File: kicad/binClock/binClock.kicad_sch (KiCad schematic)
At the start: 2 parts, among them U1 ESP32-C3_SUPERMINI, U2 LOGIC-74HC595N_DIP16_

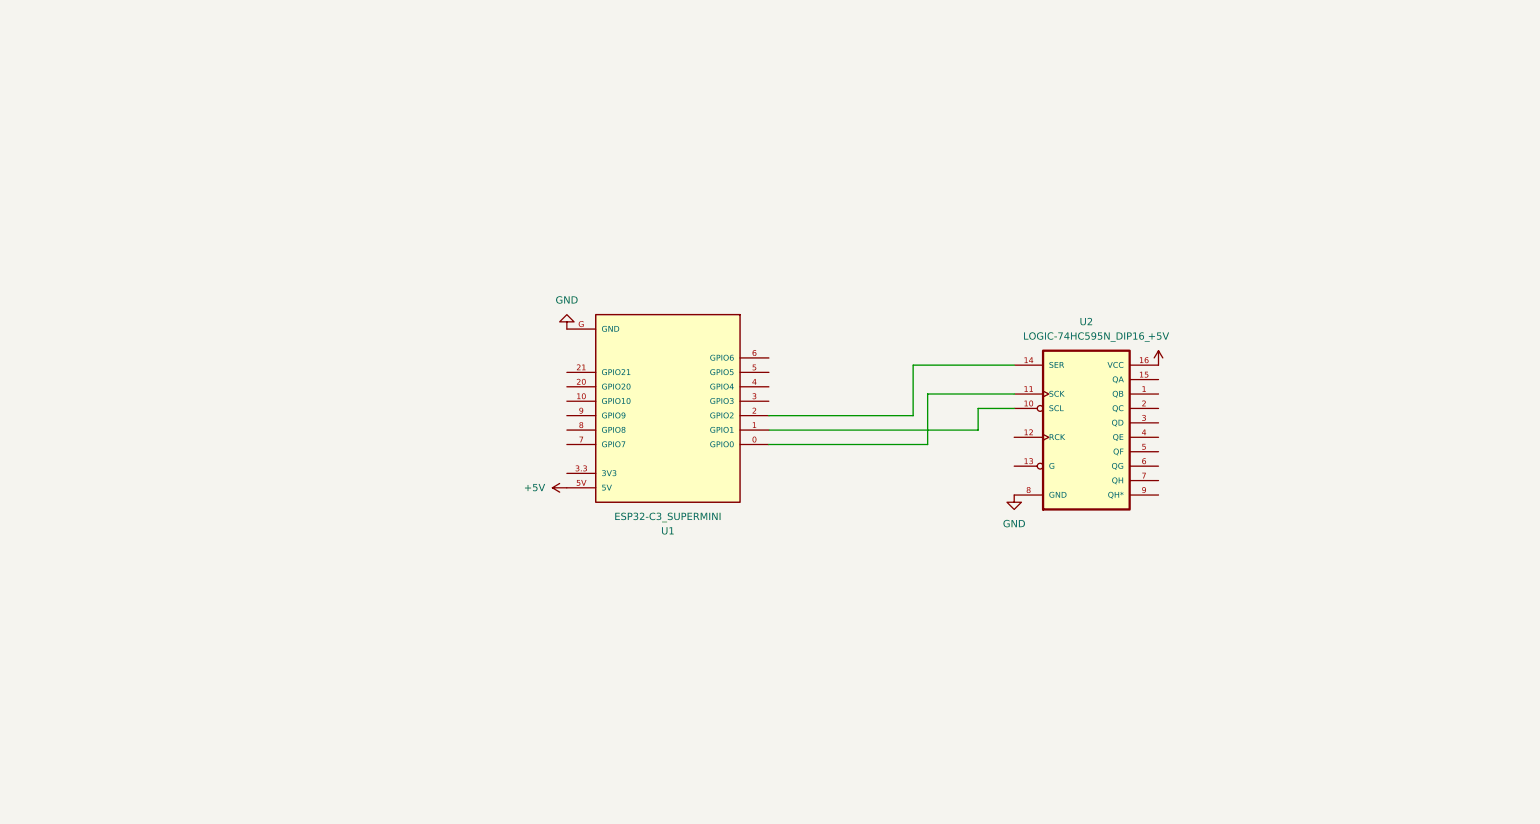
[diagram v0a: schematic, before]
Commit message: Work on schematic, added chip image
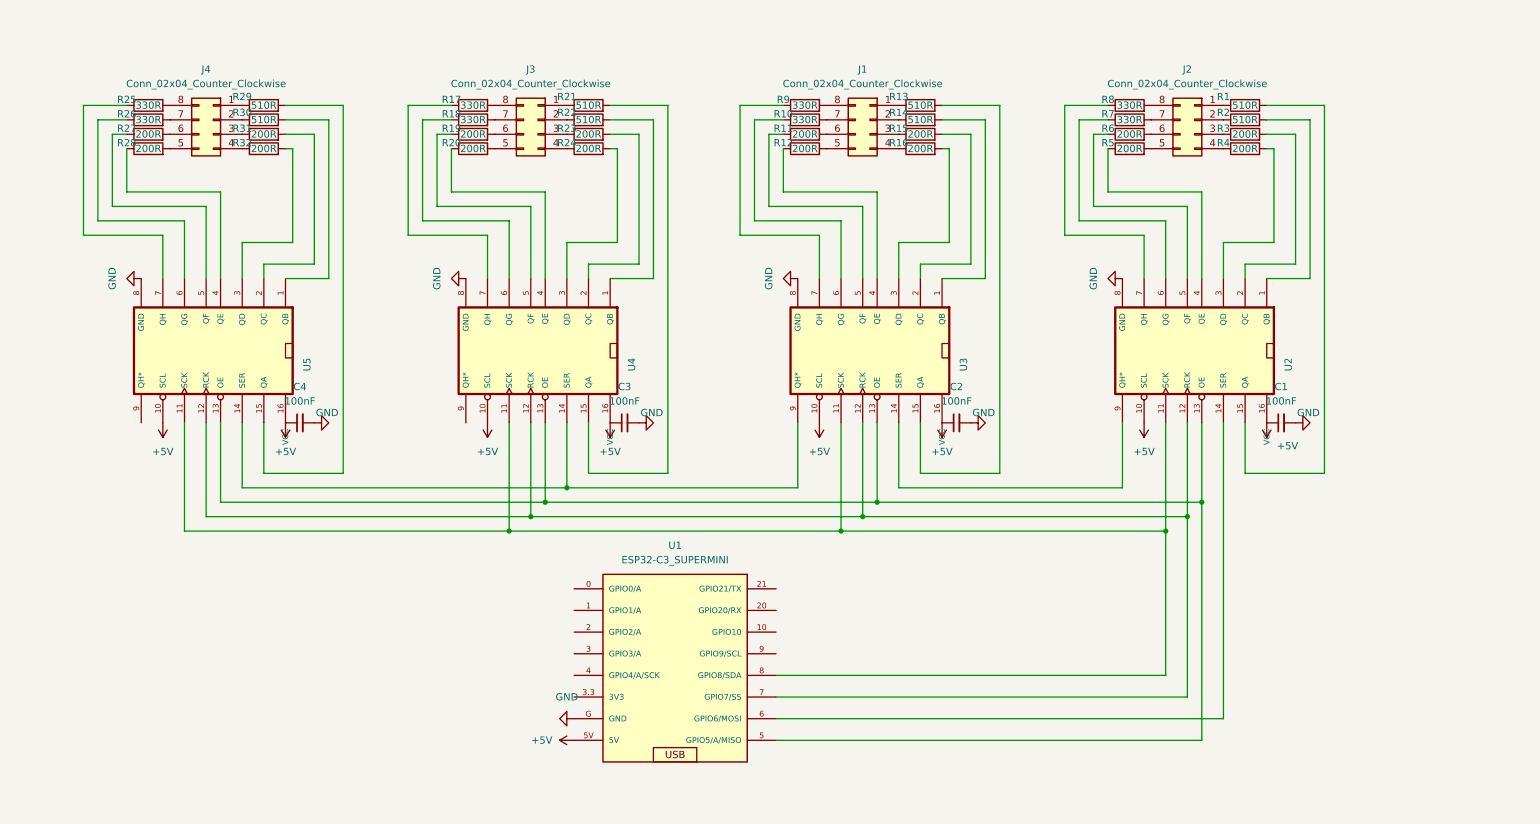
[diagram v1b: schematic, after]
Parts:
- removed U2: LOGIC-74HC595N_DIP16_, footprints:DIP16-2.54-20.32X5.84MM, symbol LOGIC-74HC595N_DIP16_:LOGIC-74HC595N_DIP16_
- added C1, C2, C3, C4: 100nF, Capacitor_THT:C_Disc_D4.3mm_W1.9mm_P5.00mm, symbol Device:C_Small
- added J1, J2, J3, J4: Conn_02x04_Counter_Clockwise, Connector_PinHeader_2.54mm:PinHeader_2x04_P2.54mm_Vertical, symbol Connector_Generic:Conn_02x04_Counter_Clockwise
- added R1, R13, R14, R2, R21, R22, R29, R30: 510R, Resistor_THT:R_Axial_DIN0207_L6.3mm_D2.5mm_P10.16mm_Horizontal, symbol Device:R
- added R10, R17, R18, R25, R26, R7, R8, R9: 330R, Resistor_THT:R_Axial_DIN0207_L6.3mm_D2.5mm_P10.16mm_Horizontal, symbol Device:R
- added R11, R12, R15, R16, R19, R20, R23, R24, R27, R28, R3, R31, R32, R4, R5, R6: 200R, Resistor_THT:R_Axial_DIN0207_L6.3mm_D2.5mm_P10.16mm_Horizontal, symbol Device:R
- added U2, U3, U4, U5: ~, symbol LOGIC-74HC595N_DIP16_:74HC595N_DIP16
- U1: footprint footprints:MODULE_ESP32-C3_SUPERMINI -> (none); Availability Not in stock -> (none); Check_prices https://www.snapeda.com/parts/ESP32-C3%20SuperMini/Espressi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 -> (none); Description_1 Super tiny ESP32-C3 board -> (none); MANUFACTURER Espressif -> (none); MAXIMUM_PACKAGE_HEIGHT 4.2mm -> (none); MF Espressif Systems -> (none); MP ESP32-C3 SuperMini -> (none); Package Package -> (none); Price None -> (none); STANDARD Manufacturer Recommendations -> (none); SnapEDA_Link https://www.snapeda.com/parts/ESP32-C3%20SuperMini/Espressi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 -> (none)
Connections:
- net +5V: now also C1.1, C2.1, C3.1, C4.1, U2.10 (SCL), U3.10 (SCL), U4.10 (SCL), U5.10 (SCL)
- net GND: now also C1.2, C2.2, C3.2, C4.2, U2.8 (GND), U3.8 (GND), U4.8 (GND), U5.8 (GND)
- net at U1.5 (GPIO5/A/MISO): now also U2.13 (OE), U3.13 (OE), U4.13 (OE), U5.13 (OE)
- net at U1.6 (GPIO6/MOSI): now also U2.14 (SER)
- net at U1.7 (GPIO7/SS): now also U2.12 (RCK), U3.12 (RCK), U4.12 (RCK), U5.12 (RCK)
- net at U1.8 (GPIO8/SDA): now also U2.11 (SCK), U3.11 (SCK), U4.11 (SCK), U5.11 (SCK)
- new net: R6.1, U2.5 (QF)
- new net: J2.6 (Pin_6), R6.2
- new net: J3.2 (Pin_2), R22.1
- new net: R22.2, U4.1 (QB)
- new net: R10.1, U3.6 (QG)
- new net: J1.7 (Pin_7), R10.2
- new net: J3.1 (Pin_1), R21.1
- new net: J3.3 (Pin_3), R23.1
- new net: J3.4 (Pin_4), R24.1
- new net: J3.5 (Pin_5), R20.2
- new net: J3.6 (Pin_6), R19.2
- new net: J3.7 (Pin_7), R18.2
- new net: J3.8 (Pin_8), R17.2
- new net: R19.1, U4.5 (QF)
- new net: R25.1, U5.7 (QH)
- new net: J4.8 (Pin_8), R25.2
- new net: J2.4 (Pin_4), R4.1
- new net: R4.2, U2.3 (QD)
- new net: J1.4 (Pin_4), R16.1
- new net: R16.2, U3.3 (QD)
- new net: R14.2, U3.1 (QB)
- new net: U2.9 (QH*), U3.14 (SER)
- new net: R13.2, U3.15 (QA)
- new net: R15.2, U3.2 (QC)
- new net: R12.1, U3.4 (QE)
- new net: R11.1, U3.5 (QF)
- new net: R9.1, U3.7 (QH)
- new net: U3.9 (QH*), U4.14 (SER), U5.14 (SER)
- new net: J1.6 (Pin_6), R11.2
- new net: R28.1, U5.4 (QE)
- new net: J4.5 (Pin_5), R28.2
- new net: R8.1, U2.7 (QH)
- new net: J2.8 (Pin_8), R8.2
- new net: R5.1, U2.4 (QE)
- new net: J2.5 (Pin_5), R5.2
- new net: J1.2 (Pin_2), R14.1
- new net: J1.3 (Pin_3), R15.1
- new net: R27.1, U5.5 (QF)
- new net: J4.6 (Pin_6), R27.2
- new net: J4.4 (Pin_4), R32.1
- new net: R32.2, U5.3 (QD)
- new net: J1.1 (Pin_1), R13.1
- new net: J1.5 (Pin_5), R12.2
- new net: J1.8 (Pin_8), R9.2
- new net: R20.1, U4.4 (QE)
- new net: R17.1, U4.7 (QH)
- new net: R23.2, U4.2 (QC)
- new net: J4.1 (Pin_1), R29.1
- new net: R29.2, U5.15 (QA)
- new net: R26.1, U5.6 (QG)
- new net: J4.7 (Pin_7), R26.2
- new net: R21.2, U4.15 (QA)
- new net: J2.1 (Pin_1), R1.1
- new net: J2.2 (Pin_2), R2.1
- new net: J2.3 (Pin_3), R3.1
- new net: J2.7 (Pin_7), R7.2
- new net: R24.2, U4.3 (QD)
- new net: J4.3 (Pin_3), R31.1
- new net: R31.2, U5.2 (QC)
- new net: R7.1, U2.6 (QG)
- new net: J4.2 (Pin_2), R30.1
- new net: R30.2, U5.1 (QB)
- new net: R2.2, U2.1 (QB)
- new net: R18.1, U4.6 (QG)
- new net: R3.2, U2.2 (QC)
- new net: R1.2, U2.15 (QA)

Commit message: Finished schematic and board layout. Included gerbers. Ordered board from jlcpcb.
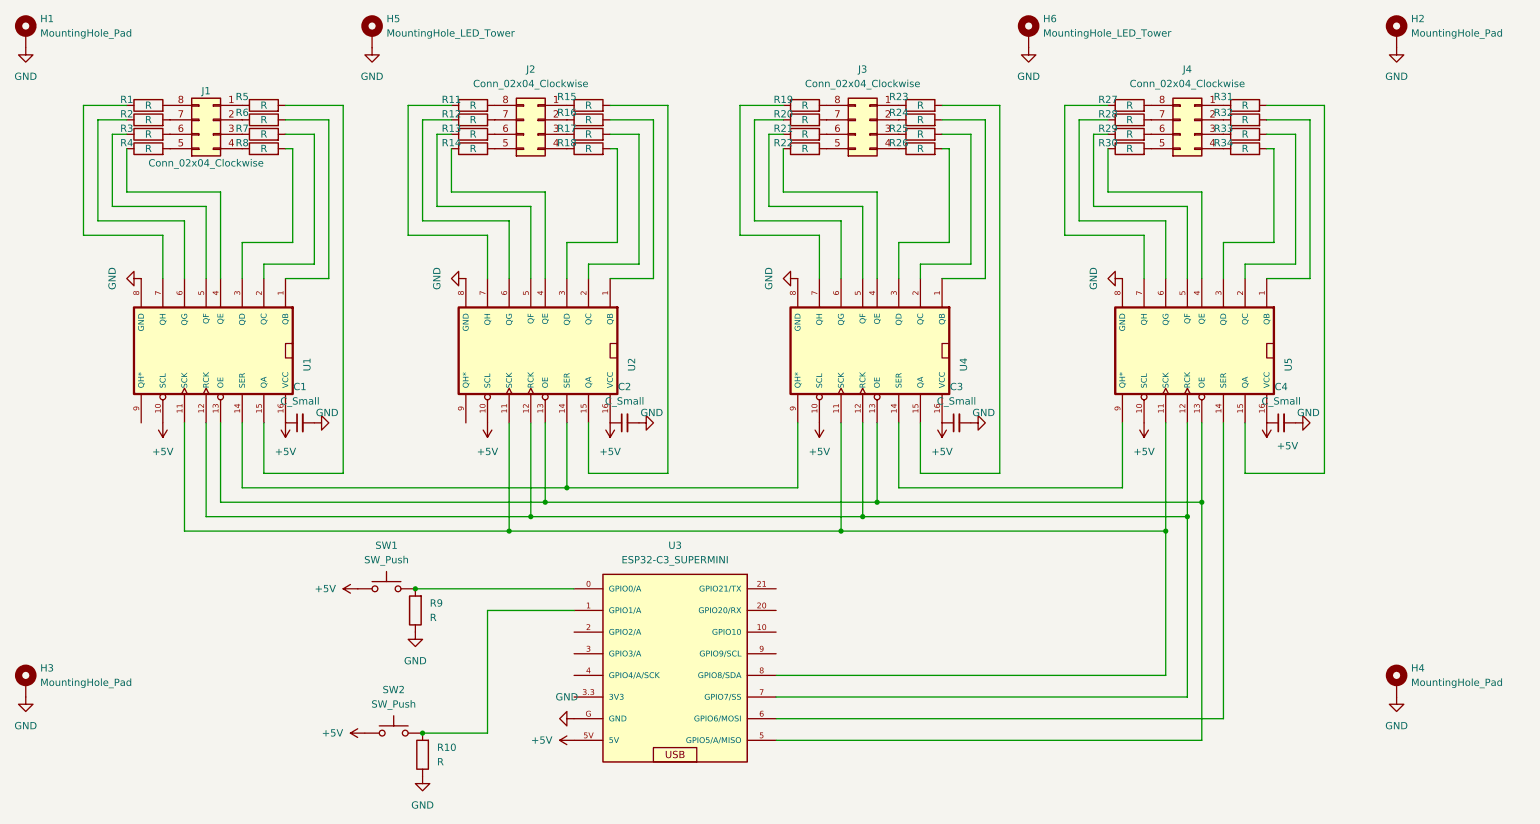
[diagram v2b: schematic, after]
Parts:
- added H1, H2, H3, H4: MountingHole_Pad, MountingHole:MountingHole_2.7mm_M2.5_Pad_TopBottom, symbol Mechanical:MountingHole_Pad
- added H5, H6: MountingHole_LED_Tower, MountingHole:MountingHole_2.2mm_M2_Pad_TopBottom, symbol Mechanical:MountingHole_Pad
- added R10, R9: R, Resistor_THT:R_Axial_DIN0207_L6.3mm_D2.5mm_P7.62mm_Horizontal, symbol Device:R
- added SW1, SW2: SW_Push, Button_Switch_THT:SW_PUSH_6mm, symbol Switch:SW_Push
- C1: renamed from C4; value 100nF -> C_Small; footprint Capacitor_THT:C_Disc_D4.3mm_W1.9mm_P5.00mm -> Capacitor_THT:C_Disc_D3.0mm_W1.6mm_P2.50mm
- C2: renamed from C3; value 100nF -> C_Small; footprint Capacitor_THT:C_Disc_D4.3mm_W1.9mm_P5.00mm -> Capacitor_THT:C_Disc_D3.0mm_W1.6mm_P2.50mm
- C3: renamed from C2; value 100nF -> C_Small; footprint Capacitor_THT:C_Disc_D4.3mm_W1.9mm_P5.00mm -> Capacitor_THT:C_Disc_D3.0mm_W1.6mm_P2.50mm
- C4: renamed from C1; value 100nF -> C_Small; footprint Capacitor_THT:C_Disc_D4.3mm_W1.9mm_P5.00mm -> Capacitor_THT:C_Disc_D3.0mm_W1.6mm_P2.50mm
- J1: renamed from J4; value Conn_02x04_Counter_Clockwise -> Conn_02x04_Clockwise; footprint Connector_PinHeader_2.54mm:PinHeader_2x04_P2.54mm_Vertical -> footprints:PinHeader_2x04_P2.54mm_Vertical_Clockwise; symbol Connector_Generic:Conn_02x04_Counter_Clockwise -> conn_02x04_clockwise:Conn_02x04_Clockwise
- J2: renamed from J3; value Conn_02x04_Counter_Clockwise -> Conn_02x04_Clockwise; footprint Connector_PinHeader_2.54mm:PinHeader_2x04_P2.54mm_Vertical -> footprints:PinHeader_2x04_P2.54mm_Vertical_Clockwise; symbol Connector_Generic:Conn_02x04_Counter_Clockwise -> conn_02x04_clockwise:Conn_02x04_Clockwise
- J3: renamed from J1; value Conn_02x04_Counter_Clockwise -> Conn_02x04_Clockwise; footprint Connector_PinHeader_2.54mm:PinHeader_2x04_P2.54mm_Vertical -> footprints:PinHeader_2x04_P2.54mm_Vertical_Clockwise; symbol Connector_Generic:Conn_02x04_Counter_Clockwise -> conn_02x04_clockwise:Conn_02x04_Clockwise
- J4: renamed from J2; value Conn_02x04_Counter_Clockwise -> Conn_02x04_Clockwise; footprint Connector_PinHeader_2.54mm:PinHeader_2x04_P2.54mm_Vertical -> footprints:PinHeader_2x04_P2.54mm_Vertical_Clockwise; symbol Connector_Generic:Conn_02x04_Counter_Clockwise -> conn_02x04_clockwise:Conn_02x04_Clockwise
- R1: renamed from R25; value 330R -> R; footprint Resistor_THT:R_Axial_DIN0207_L6.3mm_D2.5mm_P10.16mm_Horizontal -> Resistor_THT:R_Axial_DIN0207_L6.3mm_D2.5mm_P7.62mm_Horizontal
- R11: renamed from R17; value 330R -> R; footprint Resistor_THT:R_Axial_DIN0207_L6.3mm_D2.5mm_P10.16mm_Horizontal -> Resistor_THT:R_Axial_DIN0207_L6.3mm_D2.5mm_P7.62mm_Horizontal
- R12: renamed from R18; value 330R -> R; footprint Resistor_THT:R_Axial_DIN0207_L6.3mm_D2.5mm_P10.16mm_Horizontal -> Resistor_THT:R_Axial_DIN0207_L6.3mm_D2.5mm_P7.62mm_Horizontal
- R13: renamed from R19; value 200R -> R; footprint Resistor_THT:R_Axial_DIN0207_L6.3mm_D2.5mm_P10.16mm_Horizontal -> Resistor_THT:R_Axial_DIN0207_L6.3mm_D2.5mm_P7.62mm_Horizontal
- R14: renamed from R20; value 200R -> R; footprint Resistor_THT:R_Axial_DIN0207_L6.3mm_D2.5mm_P10.16mm_Horizontal -> Resistor_THT:R_Axial_DIN0207_L6.3mm_D2.5mm_P7.62mm_Horizontal
- R15: renamed from R21; value 510R -> R; footprint Resistor_THT:R_Axial_DIN0207_L6.3mm_D2.5mm_P10.16mm_Horizontal -> Resistor_THT:R_Axial_DIN0207_L6.3mm_D2.5mm_P7.62mm_Horizontal
- R16: renamed from R22; value 510R -> R; footprint Resistor_THT:R_Axial_DIN0207_L6.3mm_D2.5mm_P10.16mm_Horizontal -> Resistor_THT:R_Axial_DIN0207_L6.3mm_D2.5mm_P7.62mm_Horizontal
- R17: renamed from R23; value 200R -> R; footprint Resistor_THT:R_Axial_DIN0207_L6.3mm_D2.5mm_P10.16mm_Horizontal -> Resistor_THT:R_Axial_DIN0207_L6.3mm_D2.5mm_P7.62mm_Horizontal
- R18: renamed from R24; value 200R -> R; footprint Resistor_THT:R_Axial_DIN0207_L6.3mm_D2.5mm_P10.16mm_Horizontal -> Resistor_THT:R_Axial_DIN0207_L6.3mm_D2.5mm_P7.62mm_Horizontal
- R19: renamed from R9; value 330R -> R; footprint Resistor_THT:R_Axial_DIN0207_L6.3mm_D2.5mm_P10.16mm_Horizontal -> Resistor_THT:R_Axial_DIN0207_L6.3mm_D2.5mm_P7.62mm_Horizontal
- R2: renamed from R26; value 330R -> R; footprint Resistor_THT:R_Axial_DIN0207_L6.3mm_D2.5mm_P10.16mm_Horizontal -> Resistor_THT:R_Axial_DIN0207_L6.3mm_D2.5mm_P7.62mm_Horizontal
- R20: renamed from R10; value 330R -> R; footprint Resistor_THT:R_Axial_DIN0207_L6.3mm_D2.5mm_P10.16mm_Horizontal -> Resistor_THT:R_Axial_DIN0207_L6.3mm_D2.5mm_P7.62mm_Horizontal
- R21: renamed from R11; value 200R -> R; footprint Resistor_THT:R_Axial_DIN0207_L6.3mm_D2.5mm_P10.16mm_Horizontal -> Resistor_THT:R_Axial_DIN0207_L6.3mm_D2.5mm_P7.62mm_Horizontal
- R22: renamed from R12; value 200R -> R; footprint Resistor_THT:R_Axial_DIN0207_L6.3mm_D2.5mm_P10.16mm_Horizontal -> Resistor_THT:R_Axial_DIN0207_L6.3mm_D2.5mm_P7.62mm_Horizontal
- R23: renamed from R13; value 510R -> R; footprint Resistor_THT:R_Axial_DIN0207_L6.3mm_D2.5mm_P10.16mm_Horizontal -> Resistor_THT:R_Axial_DIN0207_L6.3mm_D2.5mm_P7.62mm_Horizontal
- R24: renamed from R14; value 510R -> R; footprint Resistor_THT:R_Axial_DIN0207_L6.3mm_D2.5mm_P10.16mm_Horizontal -> Resistor_THT:R_Axial_DIN0207_L6.3mm_D2.5mm_P7.62mm_Horizontal
- R25: renamed from R15; value 200R -> R; footprint Resistor_THT:R_Axial_DIN0207_L6.3mm_D2.5mm_P10.16mm_Horizontal -> Resistor_THT:R_Axial_DIN0207_L6.3mm_D2.5mm_P7.62mm_Horizontal
- R26: renamed from R16; value 200R -> R; footprint Resistor_THT:R_Axial_DIN0207_L6.3mm_D2.5mm_P10.16mm_Horizontal -> Resistor_THT:R_Axial_DIN0207_L6.3mm_D2.5mm_P7.62mm_Horizontal
- R27: renamed from R8; value 330R -> R; footprint Resistor_THT:R_Axial_DIN0207_L6.3mm_D2.5mm_P10.16mm_Horizontal -> Resistor_THT:R_Axial_DIN0207_L6.3mm_D2.5mm_P7.62mm_Horizontal
- R28: renamed from R7; value 330R -> R; footprint Resistor_THT:R_Axial_DIN0207_L6.3mm_D2.5mm_P10.16mm_Horizontal -> Resistor_THT:R_Axial_DIN0207_L6.3mm_D2.5mm_P7.62mm_Horizontal
- R29: renamed from R6; value 200R -> R; footprint Resistor_THT:R_Axial_DIN0207_L6.3mm_D2.5mm_P10.16mm_Horizontal -> Resistor_THT:R_Axial_DIN0207_L6.3mm_D2.5mm_P7.62mm_Horizontal
- R3: renamed from R27; value 200R -> R; footprint Resistor_THT:R_Axial_DIN0207_L6.3mm_D2.5mm_P10.16mm_Horizontal -> Resistor_THT:R_Axial_DIN0207_L6.3mm_D2.5mm_P7.62mm_Horizontal
- R30: renamed from R5; value 200R -> R; footprint Resistor_THT:R_Axial_DIN0207_L6.3mm_D2.5mm_P10.16mm_Horizontal -> Resistor_THT:R_Axial_DIN0207_L6.3mm_D2.5mm_P7.62mm_Horizontal
- R31: renamed from R1; value 510R -> R; footprint Resistor_THT:R_Axial_DIN0207_L6.3mm_D2.5mm_P10.16mm_Horizontal -> Resistor_THT:R_Axial_DIN0207_L6.3mm_D2.5mm_P7.62mm_Horizontal
- R32: renamed from R2; value 510R -> R; footprint Resistor_THT:R_Axial_DIN0207_L6.3mm_D2.5mm_P10.16mm_Horizontal -> Resistor_THT:R_Axial_DIN0207_L6.3mm_D2.5mm_P7.62mm_Horizontal
- R33: renamed from R3; value 200R -> R; footprint Resistor_THT:R_Axial_DIN0207_L6.3mm_D2.5mm_P10.16mm_Horizontal -> Resistor_THT:R_Axial_DIN0207_L6.3mm_D2.5mm_P7.62mm_Horizontal
- R34: renamed from R4; value 200R -> R; footprint Resistor_THT:R_Axial_DIN0207_L6.3mm_D2.5mm_P10.16mm_Horizontal -> Resistor_THT:R_Axial_DIN0207_L6.3mm_D2.5mm_P7.62mm_Horizontal
- R4: renamed from R28; value 200R -> R; footprint Resistor_THT:R_Axial_DIN0207_L6.3mm_D2.5mm_P10.16mm_Horizontal -> Resistor_THT:R_Axial_DIN0207_L6.3mm_D2.5mm_P7.62mm_Horizontal
- R5: renamed from R29; value 510R -> R; footprint Resistor_THT:R_Axial_DIN0207_L6.3mm_D2.5mm_P10.16mm_Horizontal -> Resistor_THT:R_Axial_DIN0207_L6.3mm_D2.5mm_P7.62mm_Horizontal
- R6: renamed from R30; value 510R -> R; footprint Resistor_THT:R_Axial_DIN0207_L6.3mm_D2.5mm_P10.16mm_Horizontal -> Resistor_THT:R_Axial_DIN0207_L6.3mm_D2.5mm_P7.62mm_Horizontal
- R7: renamed from R31; value 200R -> R; footprint Resistor_THT:R_Axial_DIN0207_L6.3mm_D2.5mm_P10.16mm_Horizontal -> Resistor_THT:R_Axial_DIN0207_L6.3mm_D2.5mm_P7.62mm_Horizontal
- R8: renamed from R32; value 200R -> R; footprint Resistor_THT:R_Axial_DIN0207_L6.3mm_D2.5mm_P10.16mm_Horizontal -> Resistor_THT:R_Axial_DIN0207_L6.3mm_D2.5mm_P7.62mm_Horizontal
- U1: renamed from U5; footprint (none) -> footprints:DIP16-2.54-20.32X5.84MM
- U2: renamed from U4; footprint (none) -> footprints:DIP16-2.54-20.32X5.84MM
- U3: renamed from U1; footprint (none) -> footprints:MODULE_ESP32-C3_SUPERMINI
- U4: renamed from U3; footprint (none) -> footprints:DIP16-2.54-20.32X5.84MM
- U5: renamed from U2; footprint (none) -> footprints:DIP16-2.54-20.32X5.84MM
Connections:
- net +5V: now also U1.16 (VCC), U2.16 (VCC), U4.16 (VCC), U5.16 (VCC), SW1.1, SW2.1
- net GND: now also H1.1, H2.1, H3.1, H4.1, H5.1, H6.1, R10.1, R9.1
- net at U3.0 (GPIO0/A): now also R9.2, SW1.2
- net at U3.1 (GPIO1/A): now also R10.2, SW2.2
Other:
- company: (none) -> Daniel Colon
- title: (none) -> binClock
- moved on the sheet: U1, U2, U4, U5
